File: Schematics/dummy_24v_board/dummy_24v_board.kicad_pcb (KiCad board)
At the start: 2 copper layers, 69.5 x 60 mm, 8 parts, among them J1 Stack Male Edge Connector, J2 Conn_01x02_Socket, J3 Conn_01x02_Socket, J4 Conn_01x02_Socket

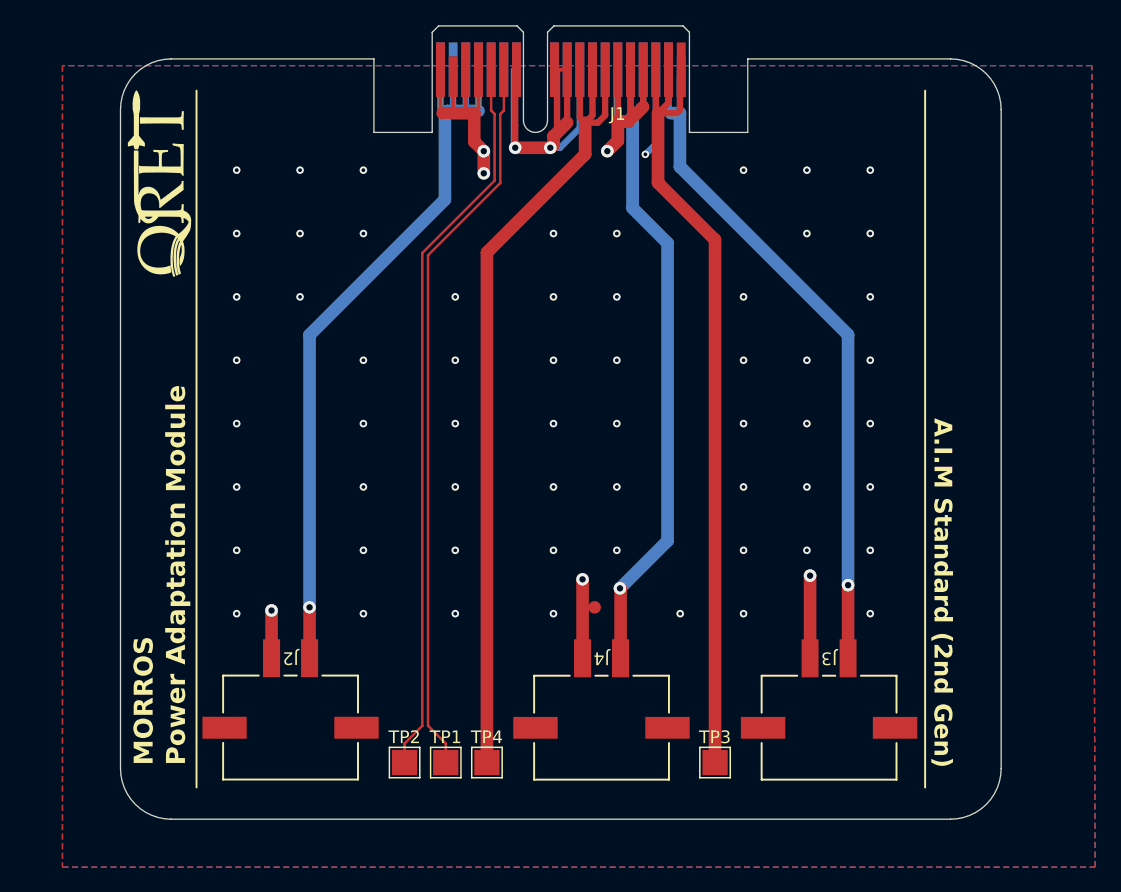
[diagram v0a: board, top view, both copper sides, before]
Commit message: cleanup PCB, switch to solid copper pour, add GND tp, and updated silkscreen
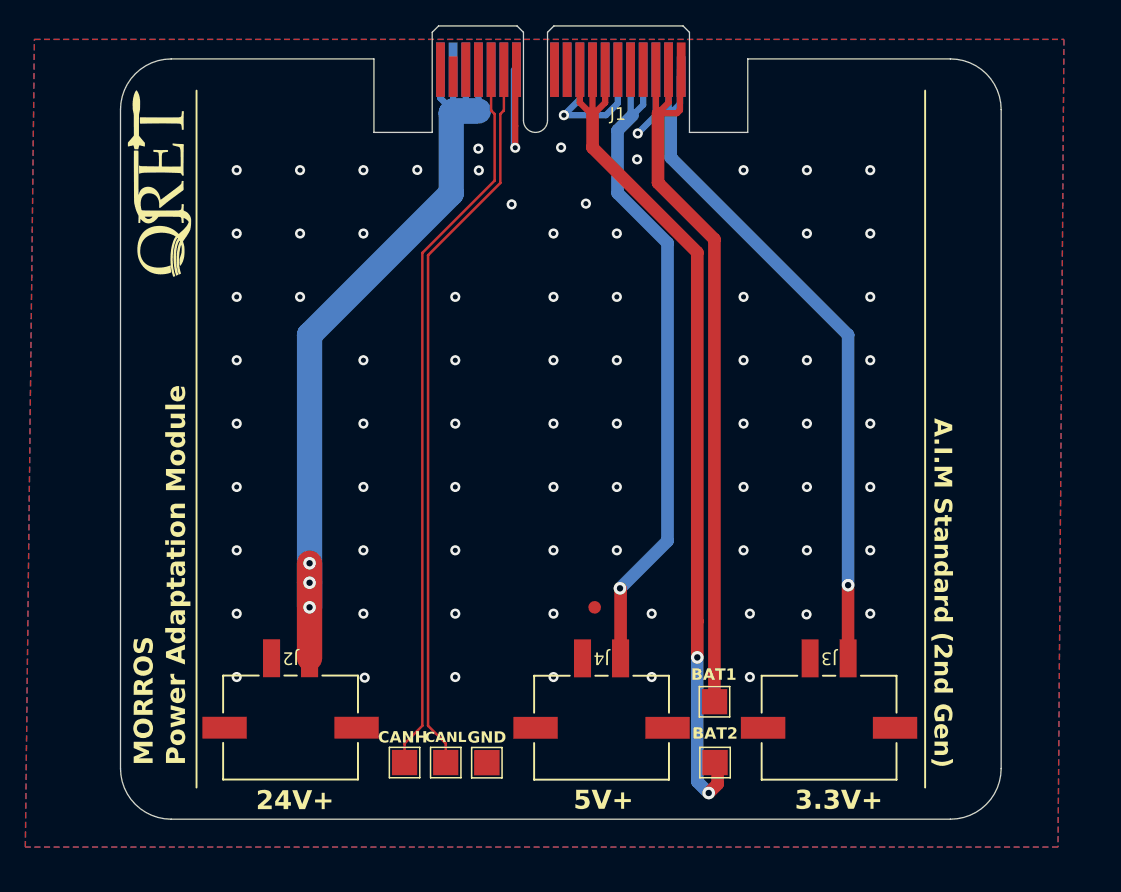
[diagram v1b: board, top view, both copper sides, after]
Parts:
- added GND: TestPoint, TestPoint:TestPoint_Pad_2.0x2.0mm, F.Cu at (51.5, 77.3)
- moved BAT1 18.6 mm to (69.5, 72.5)
- renumbered TP4 to BAT1, TP3 to BAT2, TP2 to CANH, TP1 to CANL
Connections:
- BAT1 pad 1: /BATT_2 -> /BATT_1
- BAT2 pad 1: /BATT_1 -> /BATT_2
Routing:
- net GND: track 104.0 -> 29.7 mm, vias 68 -> 76
- net /BATT_1: track 65.4 -> 60.6 mm
- net /BATT_2: track 67.9 -> 71.7 mm, vias 0 -> 2
- net +24V: track 63.4 -> 66.8 mm, vias 1 -> 3
- net +5V: track 53.2 -> 54.2 mm
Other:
- board text added: "24V+"
- board text added: "3.3V+"
- board text added: "5V+"

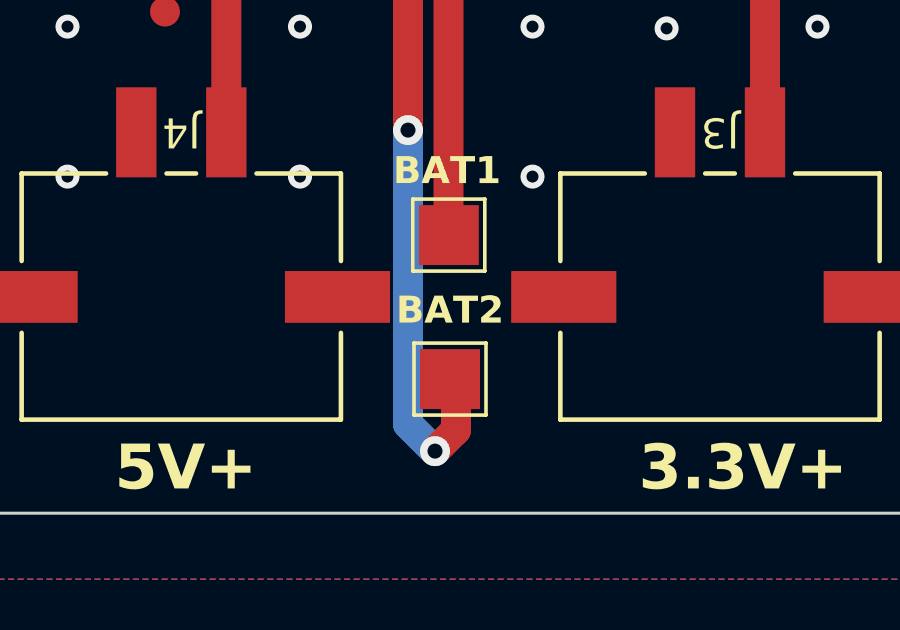
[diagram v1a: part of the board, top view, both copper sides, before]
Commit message: Update dummy_24v_board.kicad_pcb
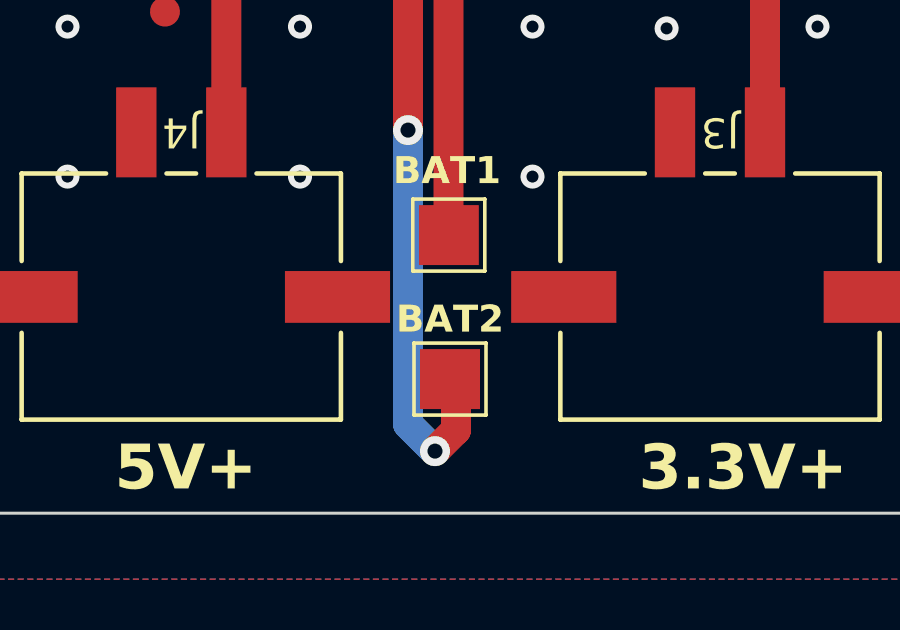
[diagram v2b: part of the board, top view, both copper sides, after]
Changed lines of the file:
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@@
 		(tags "test point SMD pad rectangle square")
 		(property "Reference" "BAT2"
-			(at 0 -2.3 0)
+			(at 0 -2 0)
 			(layer "F.SilkS")
 			(effects
@@
 		(net 7)
 		(net_name "GND")
-		(layers "F.Cu" "B.Cu")
+		(layers "F&B.Cu")
 		(hatch edge 0.5)
 		(connect_pads yes
 			(clearance 0.5)
 		)
-		(min_thickness 0.4)
+		(min_thickness 0.45)
 		(filled_areas_thickness no)
 		(fill yes

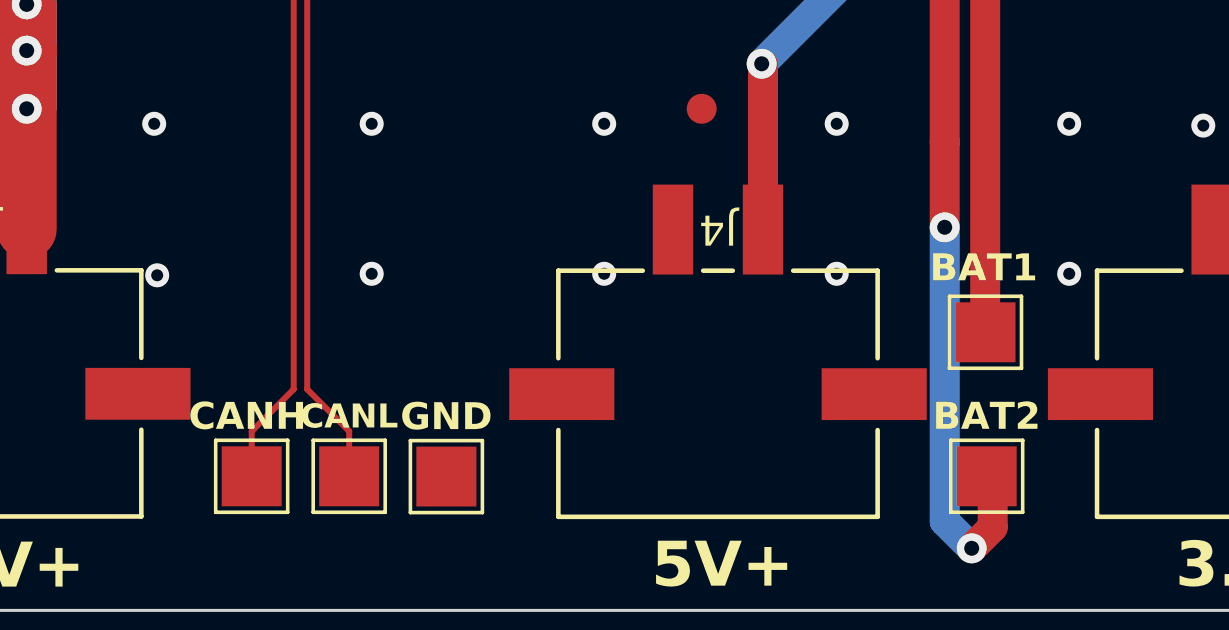
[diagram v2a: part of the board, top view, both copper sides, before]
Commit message: updates to dummy board for splitting A and B power and new edge connector
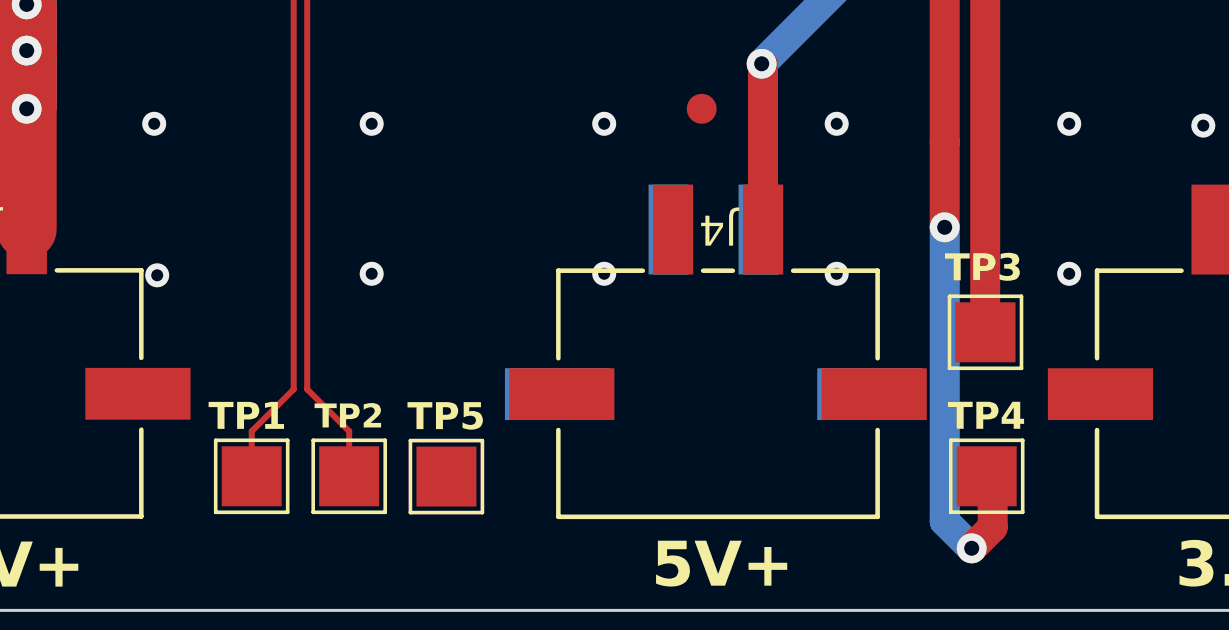
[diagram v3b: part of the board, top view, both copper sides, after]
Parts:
- added J5: Conn_01x02_Socket, footprints:CONN_2-1445057-2_TYCO, B.Cu at (58.9, 69.0)
- renumbered CANH to TP1, CANL to TP2, BAT1 to TP3, BAT2 to TP4, GND to TP5
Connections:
- J1 pad A12: GND -> GND2
- J1 pad A15: +24V -> unconnected-(J1-Reserved-PadA15)
- J1 pad A16: +24V -> unconnected-(J1-Reserved-PadA16)
- J1 pad A7: +3.3V -> +3.3V_B
- J1 pad A8: +3.3V -> +3.3V_B
- J1 pad A9: GND -> GND2
- J1 pad B10: GND -> GND2
- J1 pad B11: GND -> GND2
- J1 pad B12: GND -> GND2
- J1 pad B15: GND -> unconnected-(J1-Reserved-PadB15)
- J1 pad B16: GND -> unconnected-(J1-Reserved-PadB16)
- J1 pad B17: GND -> unconnected-(J1-Reserved-PadB17)
- J1 pad B18: GND -> unconnected-(J1-Reserved-PadB18)
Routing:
- net GND: track 29.7 -> 17.4 mm, vias 76 -> 75
- net GND2: track 0.00 -> 12.4 mm, vias 0 -> 1

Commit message: Updated PCB layout with new 3.3V_B connector
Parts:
- moved J5 0.10 mm to (59.0, 69.0)
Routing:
- net +3.3V_B: track 0.00 -> 50.0 mm
- net GND2: track 12.4 -> 18.6 mm, vias 1 -> 2
- net GND: track 17.4 -> 12.7 mm
- net +5V: track 54.2 -> 53.4 mm
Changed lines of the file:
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@@
 	(footprint "footprints:CONN_2-1445057-2_TYCO"
 		(layer "B.Cu")
-		(at 58.9 69.0249)
+		(at 59.000001 69)
 		(tags "2-1445057-2 ")
 		(property "Reference" "J5"
@@
 	)
 	(segment
-		(start 62 63.5)
-		(end 65.75 59.75)
+		(start 62.75 33.25)
+		(end 62.75 26.42)
 		(width 1)
 		(layer "B.Cu")
@@
 	)
 	(segment
-		(start 61.81 32.31)
-		(end 61.81 27.36)
+		(start 62 63.5)
+		(end 65.75 59.75)
 		(width 1)
 		(layer "B.Cu")
@@
 	)
 	(segment
-		(start 65.75 59.75)
-		(end 65.75 36.25)
-		(width 1)
+		(start 62.83 26)
+		(end 62.83 22.57)
+		(width 0.5)
 		(layer "B.Cu")
 		(net 3)
 	)
 	(segment
-		(start 61.81 27.36)
-		(end 63 26.17)
+		(start 65.75 36.25)
+		(end 62.75 33.25)
 		(width 1)
 		(layer "B.Cu")
@@
 	)
 	(segment
-		(start 62.83 26)
-		(end 62.83 22.57)
+		(start 63 26.17)
+		(end 63.83 25.34)
 		(width 0.5)
 		(layer "B.Cu")
@@
 	)
 	(segment
-		(start 63 26.17)
-		(end 63.83 25.34)
-		(width 0.5)
+		(start 62.75 26.42)
+		(end 63 26.17)
+		(width 1)
 		(layer "B.Cu")
 		(net 3)
 	)
 	(segment
-		(start 65.75 36.25)
-		(end 61.81 32.31)
+		(start 65.75 59.75)
+		(end 65.75 36.25)
 		(width 1)
 		(layer "B.Cu")
@@
 	)
 	(via
+		(at 61.5 28.75)
+		(size 0.8)
+		(drill 0.4)
+		(layers "F.Cu" "B.Cu")
+		(net 7)
+	)
+	(via
 		(at 56.75 60.5)
 		(size 0.8)
@@
 	)
 	(via
-		(at 63.4 27.6)
+		(at 63.9 28.25)
 		(size 0.8)
 		(drill 0.4)
@@
 	)
 	(via
-		(at 63.35 29.65)
+		(at 63.9 30)
 		(size 0.8)
 		(drill 0.4)
@@
 	)
 	(via
-		(at 57.57 26.16)
-		(size 0.8)
-		(drill 0.4)
-		(layers "F.Cu" "B.Cu")
-		(net 7)
-	)
-	(via
 		(at 50.86 30.52)
 		(size 0.8)
@@
 	)
 	(via
-		(at 56.75 35.5)
+		(at 54.25 37.25)
 		(size 0.8)
 		(drill 0.4)
@@
 	)
 	(via
-		(at 59.31 33.14)
+		(at 57.75 33.14)
 		(size 0.8)
 		(drill 0.4)
@@
 	)
 	(via
-		(at 57.35 28.71)
+		(at 56.25 30)
 		(size 0.8)
 		(drill 0.4)
@@
 	)
 	(segment
-		(start 63.4 27.6)
-		(end 64.83 26.17)
+		(start 61.83 25.67)
+		(end 61.83 22.57)
 		(width 0.5)
 		(layer "B.Cu")
@@
 	)
 	(segment
-		(start 58.83 24.9)
-		(end 58.83 22.57)
+		(start 61.5 28.75)
+		(end 61.5 26)
 		(width 0.5)
 		(layer "B.Cu")
@@
 	)
 	(segment
-		(start 57.57 26.16)
-		(end 60.89 26.16)
-		(width 0.5)
-		(layer "B.Cu")
-		(net 7)
-	)
-	(segment
-		(start 60.89 26.16)
-		(end 61.83 25.22)
+		(start 63.9 28.25)
+		(end 64.83 27.32)
 		(width 0.5)
 		(layer "B.Cu")
@@
 	)
 	(segment
-		(start 64.83 26.17)
+		(start 64.83 27.32)
 		(end 64.83 22.57)
 		(width 0.5)
@@
 	)
 	(segment
-		(start 57.57 26.16)
-		(end 58.83 24.9)
-		(width 0.5)
-		(layer "B.Cu")
-		(net 7)
-	)
-	(segment
-		(start 61.83 25.22)
-		(end 61.83 22.57)
+		(start 61.5 26)
+		(end 61.83 25.67)
 		(width 0.5)
 		(layer "B.Cu")
@@
 		(net 14)
 	)
+	(via
+		(at 58 28.5)
+		(size 0.8)
+		(drill 0.4)
+		(layers "F.Cu" "B.Cu")
+		(net 14)
+	)
+	(segment
+		(start 58 28.5)
+		(end 58 25.75)
+		(width 0.5)
+		(layer "B.Cu")
+		(net 14)
+	)
 	(segment
 		(start 53.73 28.73)
@@
 		(net 14)
 	)
+	(segment
+		(start 58.83 24.92)
+		(end 58.83 22.57)
+		(width 0.5)
+		(layer "B.Cu")
+		(net 14)
+	)
+	(segment
+		(start 58 25.75)
+		(end 58.83 24.92)
+		(width 0.5)
+		(layer "B.Cu")
+		(net 14)
+	)
+	(segment
+		(start 59.83 25.42)
+		(end 60.83 24.42)
+		(width 0.5)
+		(layer "B.Cu")
+		(net 15)
+	)
+	(segment
+		(start 59.83 22.57)
+		(end 59.83 25.42)
+		(width 0.5)
+		(layer "B.Cu")
+		(net 15)
+	)
+	(segment
+		(start 59.25 26)
+		(end 59.25 59.75)
+		(width 1)
+		(layer "B.Cu")
+		(net 15)
+	)
+	(segment
+		(start 60.83 24.42)
+		(end 60.83 22.57)
+		(width 0.5)
+		(layer "B.Cu")
+		(net 15)
+	)
+	(segment
+		(start 59.83 25.42)
+		(end 59.25 26)
+		(width 0.5)
+		(layer "B.Cu")
+		(net 15)
+	)
+	(segment
+		(start 59 60)
+		(end 59.000001 60.000001)
+		(width 0.5)
+		(layer "B.Cu")
+		(net 15)
+	)
+	(segment
+		(start 59.25 59.75)
+		(end 59 60)
+		(width 0.5)
+		(layer "B.Cu")
+		(net 15)
+	)
+	(segment
+		(start 59.000001 60.000001)
+		(end 59.000001 69)
+		(width 1)
+		(layer "B.Cu")
+		(net 15)
+	)
 	(zone
 		(net 7)
 		(net_name "GND")
-		(layers "F.Cu" "B.Cu")
+		(layers "F&B.Cu")
 		(hatch edge 0.5)
 		(connect_pads yes

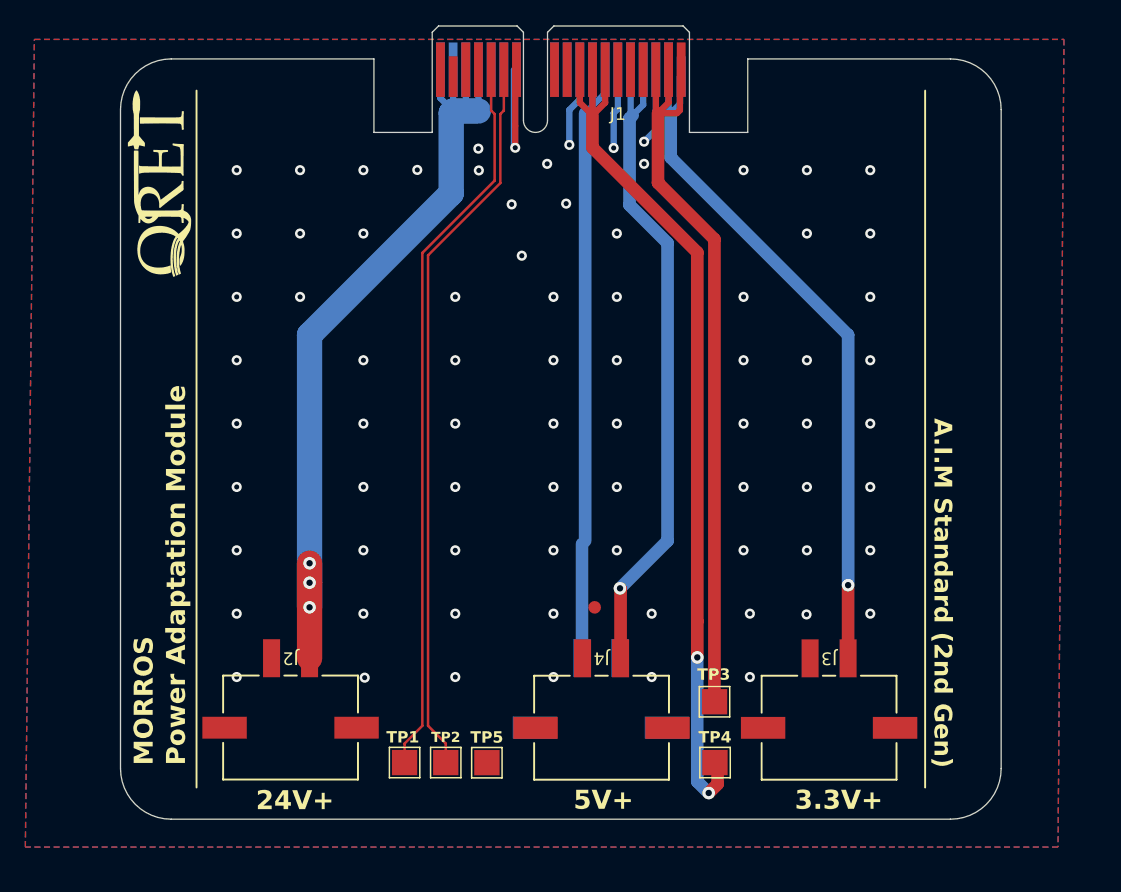
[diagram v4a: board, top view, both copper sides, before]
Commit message: 3.3V_B flipped to front & Gn2 trace added
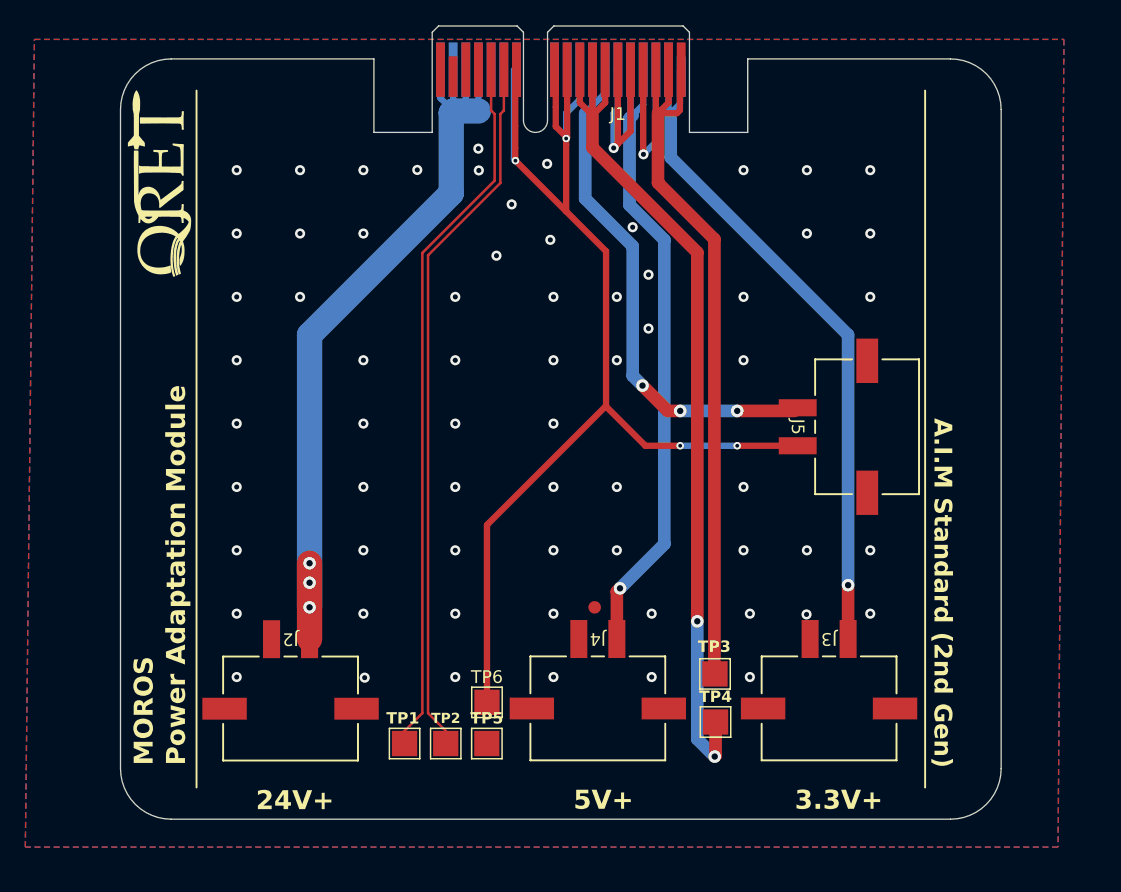
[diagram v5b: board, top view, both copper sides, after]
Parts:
- added TP6: TestPoint, TestPoint:TestPoint_Pad_2.0x2.0mm, F.Cu at (51.5, 72.5)
- J5: moved to F.Cu
- moved J5 26.1 mm to (76.0, 49.2), turned to -90 degrees
- moved TP4 3.20 mm to (69.5, 74.0)
- moved TP3 2.20 mm to (69.5, 70.2)
- moved J4 1.55 mm to (61.8, 67.5)
- moved J3 1.52 mm to (80.0, 67.5)
- moved TP5 1.51 mm to (51.5, 75.8)
- moved J2 1.50 mm to (37.5, 67.5)
- moved TP1 1.50 mm to (45.0, 75.8)
- moved TP2 1.50 mm to (48.2, 75.8)
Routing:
- net GND2: track 18.6 -> 102.4 mm, vias 2 -> 4
- net GND: track 12.7 -> 33.5 mm, vias 75 -> 68
- net +3.3V_B: track 50.0 -> 43.5 mm, vias 0 -> 3
- net /BATT_2: track 71.7 -> 69.0 mm
- net /BATT_1: track 60.6 -> 58.4 mm
- net +5V: track 53.4 -> 51.7 mm
- net +3.3V: track 55.0 -> 53.5 mm
- net +24V: track 66.8 -> 65.3 mm
- net CAN_-: track 57.7 -> 56.7 mm
- net CAN_+: track 57.7 -> 56.7 mm
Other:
- board text added: "MOROS"
- board text removed: "MORROS"

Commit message: DRC checked
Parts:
- J4: moved to B.Cu
- moved J5 23.2 mm to (61.8, 67.5), turned to 180 degrees
- moved J4 3.25 mm to (58.5, 67.5), turned to 0 degrees
- renumbered TP3 to BATT1, TP4 to BATT2, TP1 to CAN+, TP2 to CAN-, TP5 to GND, TP6 to GND2
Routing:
- net +24V: track 65.3 -> 56.7 mm
- net GND2: track 102.4 -> 96.1 mm, vias 4 -> 2
- net +3.3V_B: track 43.5 -> 49.5 mm, vias 3 -> 1
- net +5V: track 51.7 -> 50.8 mm, vias 1 -> 0
- net GND: vias 68 -> 73
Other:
- board text added: "3.3V+ B"
